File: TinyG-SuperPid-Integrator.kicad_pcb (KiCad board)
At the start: 4 copper layers, 85.7 x 48.3 mm, 25 parts, among them J1 TINYG, J2 SPP, J3 Vin, J4 UJ2-AH-4-TH, J5 SSR, U1 LM2678T-5.0, U2 TLP2662F, U3 TLP2662F

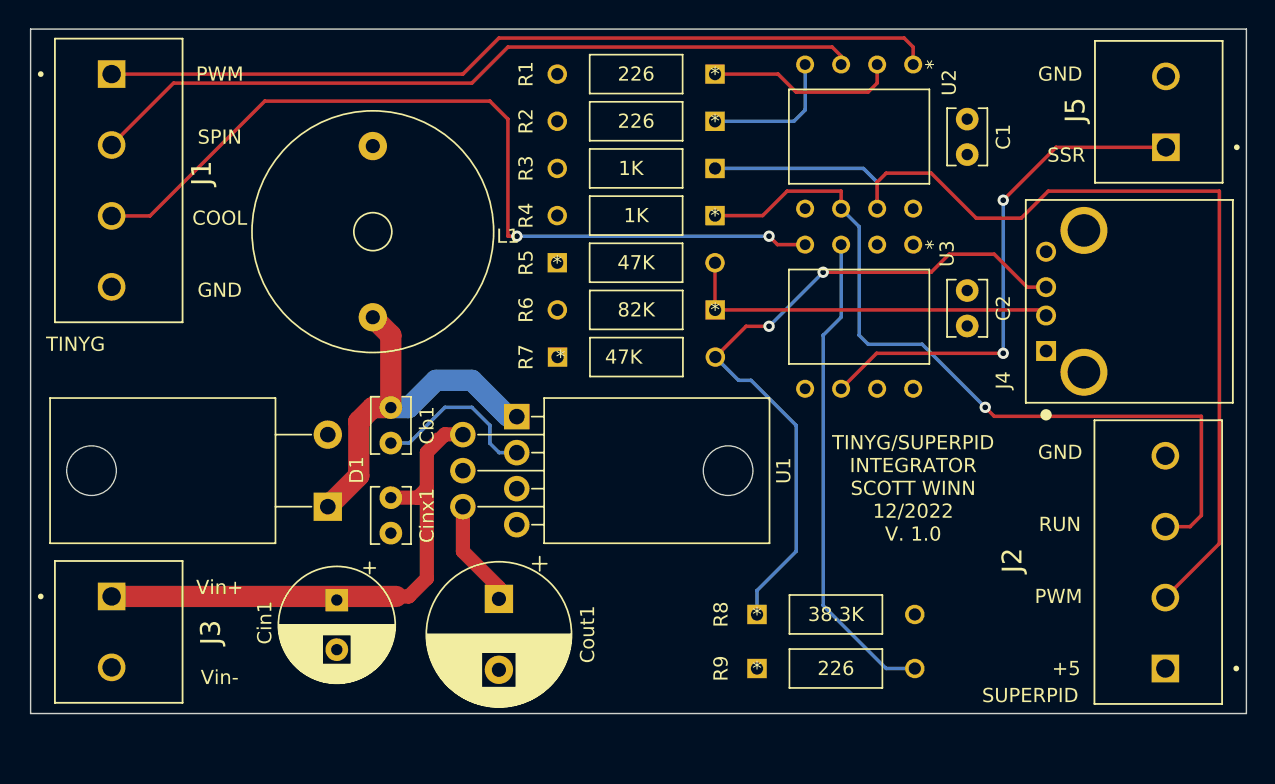
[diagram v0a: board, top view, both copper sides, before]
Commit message: Fixed backwards diode on U2, straightened internal plane boundaries (aesthetic)
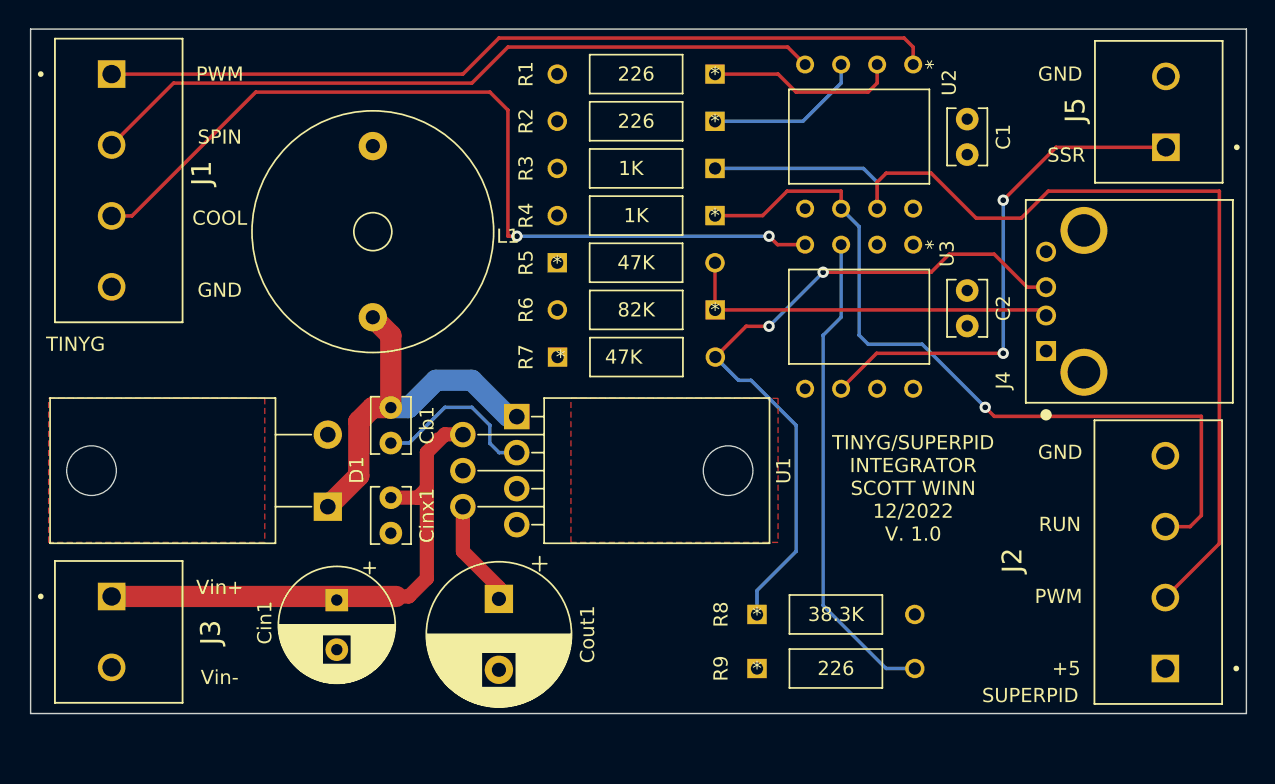
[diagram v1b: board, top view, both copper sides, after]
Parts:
- J3: value Vin -> Vin (12-26V)
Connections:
- J1 pad 2: Net-(J1-Pad2) -> Net-(U2-Pad4)
- U2 pad 3: Net-(J1-Pad2) -> Net-(R2-Pad1)
- U2 pad 4: Net-(R2-Pad1) -> Net-(U2-Pad4)
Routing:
- net Net-(J1-Pad2): track 55.2 -> 0.00 mm
- net Net-(U2-Pad4): track 0.00 -> 52.3 mm
- net Net-(R2-Pad1): track 9.89 -> 11.3 mm
- net Net-(J1-Pad3): track 61.3 -> 62.2 mm
- added copper zone on F.Cu, net (none)

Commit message: Added power LED, load resistor. Updated power supply layout.
Updated layout of power supply to shorten distances between L1, Cout, Cin, and Cb1.  Added power LED indicator and pads for a small load resistor to stabilize the switching PS if needed.
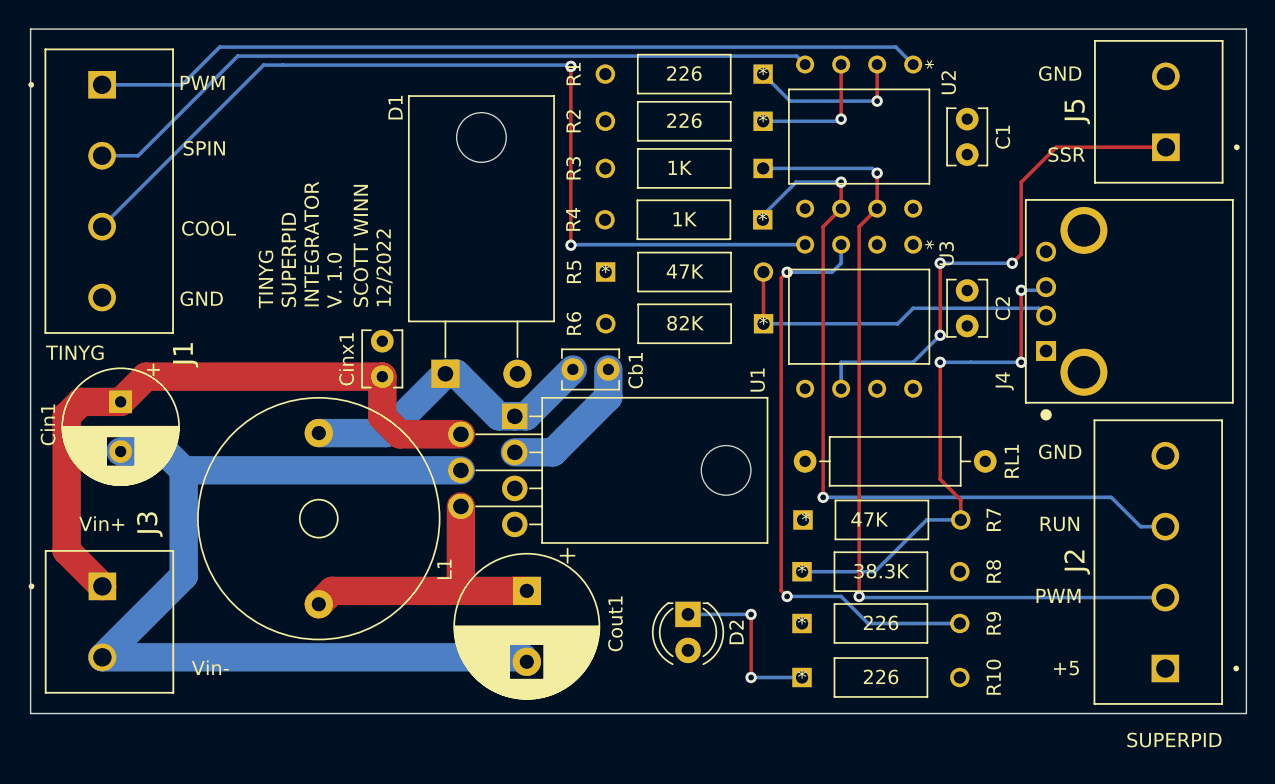
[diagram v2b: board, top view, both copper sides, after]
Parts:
- added D2: LED, LED_THT:LED_D4.0mm, F.Cu at (71.1, 86.4)
- added R10: 226, 1_MyGlobalLibFootprintLibrary:MRS25000C2260FCT00, F.Cu at (79.2, 90.8)
- added RL1: DNI, Resistor_THT:R_Axial_DIN0309_L9.0mm_D3.2mm_P12.70mm_Horizontal, F.Cu at (79.4, 75.6)
- moved R7 20.8 mm to (79.2, 79.7)
- moved Cin1 20.7 mm to (31.1, 71.4)
- moved Cb1 13.1 mm to (63.0, 69.1), turned to 0 degrees
- moved D1 12.5 mm to (54.0, 69.4), turned to 0 degrees
- moved L1 9.01 mm to (45.1, 73.6), turned to -90 degrees
- moved Cinx1 8.55 mm to (49.6, 69.6), turned to 90 degrees
- moved R9 4.49 mm to (79.2, 87.0)
- moved R8 4.38 mm to (79.2, 83.3)
- moved R6 3.55 mm to (76.4, 65.9)
- moved R5 3.48 mm to (65.3, 62.2)
- moved R1 3.39 mm to (76.4, 48.3)
- moved R2 3.39 mm to (76.4, 51.6)
- moved R3 3.39 mm to (76.4, 54.9)
- moved R4 3.38 mm to (76.4, 58.5)
- moved Cout1 2.05 mm to (59.8, 84.7)
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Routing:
- net GND: track 0.00 -> 70.1 mm
- net +5V: track 7.55 -> 21.1 mm
- net Net-(D2-Pad1): track 0.00 -> 12.5 mm, vias 0 -> 2
- net Net-(J4-Pad3): track 49.5 -> 37.1 mm, vias 2 -> 3
- net Net-(J2-Pad2): track 72.3 -> 60.2 mm, vias 0 -> 2
- net Net-(Cin1-Pad1): track 37.6 -> 45.4 mm
- net Net-(R9-Pad2): track 34.3 -> 41.6 mm, vias 0 -> 2
- net Net-(Cb1-Pad1): track 27.2 -> 22.3 mm
- net Net-(J1-Pad3): track 62.2 -> 66.9 mm
- net Net-(R1-Pad1): track 13.5 -> 11.4 mm, vias 0 -> 1
- net Net-(J2-Pad3): track 56.6 -> 54.5 mm, vias 1 -> 2
- net Net-(J4-Pad2): track 26.8 -> 24.8 mm
- net Net-(R2-Pad1): track 11.3 -> 9.41 mm, vias 0 -> 1
- net Net-(Cb1-Pad2): track 12.0 -> 10.2 mm
- net Net-(J5-Pad1): track 36.3 -> 37.0 mm, vias 2 -> 3
- removed copper zone on F.Cu, net (none)
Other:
- board text added: "SCOTT WINN 12/2022"
- board text added: "TINYG SUPERPID INTEGRATOR V. 1.0"
- board text removed: "TINYG/SUPERPID INTEGRATOR SCOTT WINN 12/2022 V. 1.0"
